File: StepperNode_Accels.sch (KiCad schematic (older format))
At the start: 0 parts

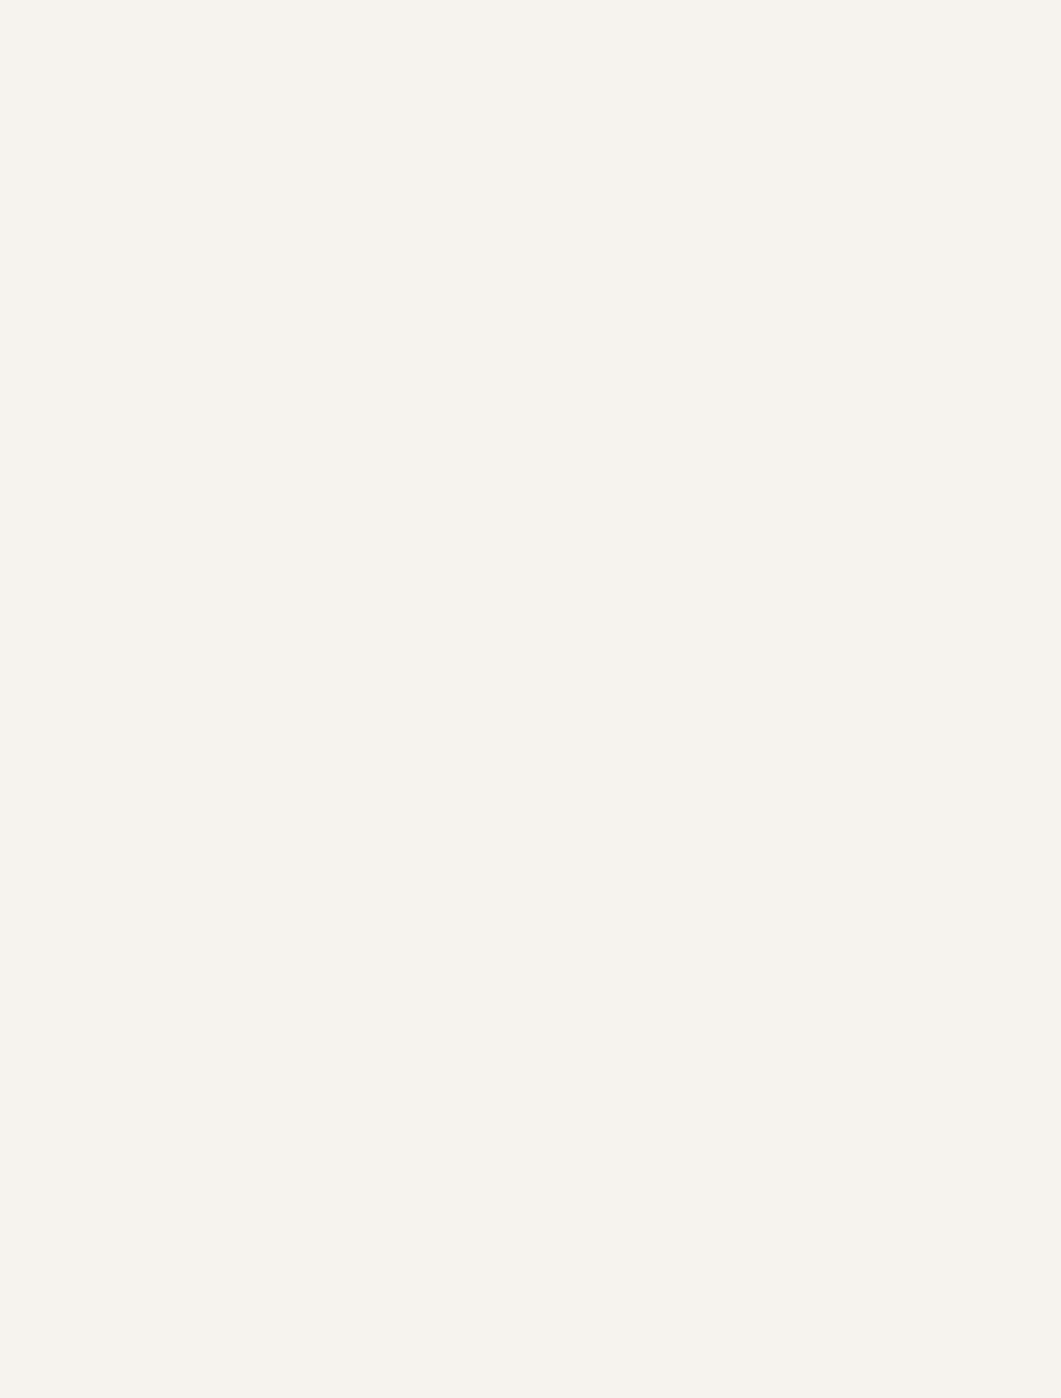
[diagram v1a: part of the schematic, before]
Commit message: Added Brake Failsafe Sheet
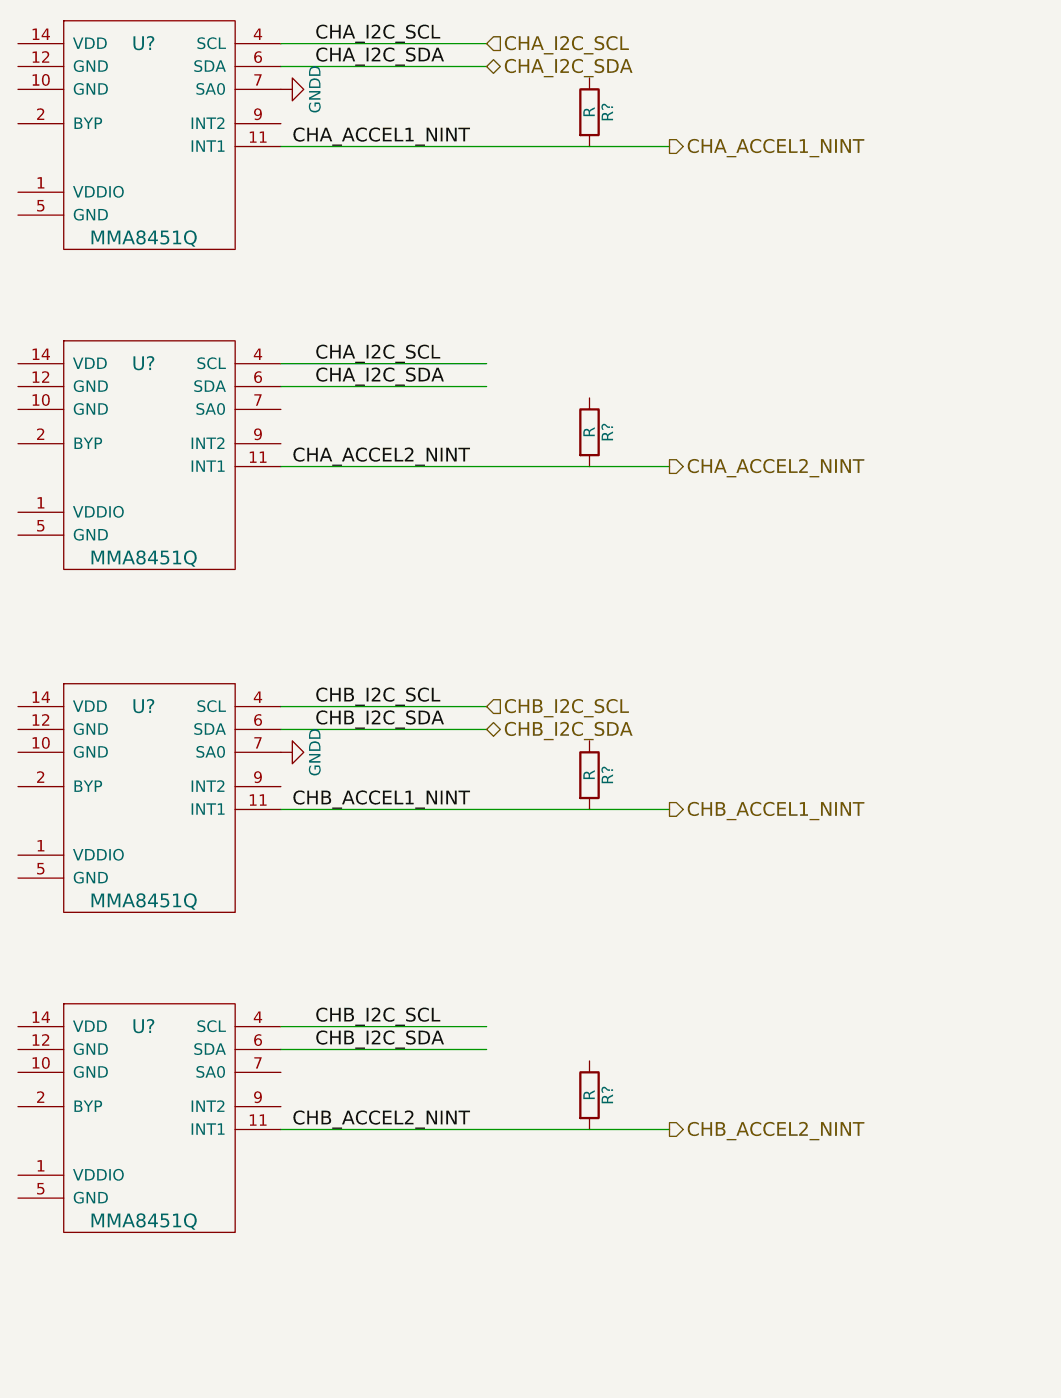
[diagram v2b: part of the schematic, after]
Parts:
- added R? (x4): R, symbol R
- added U? (x4): MMA8451Q, symbol MMA8451Q
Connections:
- net labels added: CHA_ACCEL1_NINT, CHA_ACCEL2_NINT, CHA_I2C_SCL, CHA_I2C_SDA, CHB_ACCEL1_NINT, CHB_ACCEL2_NINT, CHB_I2C_SCL, CHB_I2C_SDA, GNDD
- wire segments 0 -> 12
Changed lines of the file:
@@
 $Descr A3 16535 11693
 encoding utf-8
-Sheet 12 13
+Sheet 12 14
 Title "Accelerometers"
 Date ""
@@
 Text Notes 11950 10500 0    60   ~ 0
 Original Author: SafetyLok
+$Comp
+L MMA8451Q U?
+U 1 1 5753CAE0
+P 5300 2200
+F 0 "U?" H 5300 2700 60  0000 C CNN
+F 1 "MMA8451Q" H 5300 1850 60  0000 C CNN
+F 2 "" H 5300 2200 60  0000 C CNN
+F 3 "" H 5300 2200 60  0000 C CNN
+	1    5300 2200
+	1    0    0    -1
+$EndComp
+Wire Wire Line
+	5900 1700 6800 1700
+Wire Wire Line
+	5900 1800 6800 1800
+Text Label 6050 1700 0    60   ~ 0
+CHA_I2C_SCL
+Text Label 6050 1800 0    60   ~ 0
+CHA_I2C_SDA
+Wire Wire Line
+	5900 2150 7600 2150
+Text Label 5950 2150 0    60   ~ 0
+CHA_ACCEL1_NINT
+$Comp
+L R R?
+U 1 1 5753CBA8
+P 7250 2000
+F 0 "R?" V 7330 2000 50  0000 C CNN
+F 1 "R" V 7250 2000 50  0000 C CNN
+F 2 "" V 7180 2000 50  0000 C CNN
+F 3 "" H 7250 2000 50  0000 C CNN
+	1    7250 2000
+	1    0    0    -1
+$EndComp
+$Comp
+L MMA8451Q U?
+U 1 1 5753CD7B
+P 5300 3600
+F 0 "U?" H 5300 4100 60  0000 C CNN
+F 1 "MMA8451Q" H 5300 3250 60  0000 C CNN
+F 2 "" H 5300 3600 60  0000 C CNN
+F 3 "" H 5300 3600 60  0000 C CNN
+	1    5300 3600
+	1    0    0    -1
+$EndComp
+Wire Wire Line
+	5900 3100 6800 3100
+Wire Wire Line
+	5900 3200 6800 3200
+Text Label 6050 3100 0    60   ~ 0
+CHA_I2C_SCL
+Text Label 6050 3200 0    60   ~ 0
+CHA_I2C_SDA
+Wire Wire Line
+	5900 3550 7600 3550
+Text Label 5950 3550 0    60   ~ 0
+CHA_ACCEL2_NINT
+$Comp
+L R R?
+U 1 1 5753CD87
+P 7250 3400
+F 0 "R?" V 7330 3400 50  0000 C CNN
+F 1 "R" V 7250 3400 50  0000 C CNN
+F 2 "" V 7180 3400 50  0000 C CNN
+F 3 "" H 7250 3400 50  0000 C CNN
+	1    7250 3400
+	1    0    0    -1
+$EndComp
+$Comp
+L MMA8451Q U?
+U 1 1 5753CF5A
+P 5300 5100
+F 0 "U?" H 5300 5600 60  0000 C CNN
+F 1 "MMA8451Q" H 5300 4750 60  0000 C CNN
+F 2 "" H 5300 5100 60  0000 C CNN
+F 3 "" H 5300 5100 60  0000 C CNN
+	1    5300 5100
+	1    0    0    -1
+$EndComp
+Wire Wire Line
+	5900 4600 6800 4600
+Wire Wire Line
+	5900 4700 6800 4700
+Text Label 6050 4600 0    60   ~ 0
+CHB_I2C_SCL
+Text Label 6050 4700 0    60   ~ 0
+CHB_I2C_SDA
+Wire Wire Line
+	5900 5050 7600 5050
+Text Label 5950 5050 0    60   ~ 0
+CHB_ACCEL1_NINT
+$Comp
+L R R?
+U 1 1 5753CF66
+P 7250 4900
+F 0 "R?" V 7330 4900 50  0000 C CNN
+F 1 "R" V 7250 4900 50  0000 C CNN
+F 2 "" V 7180 4900 50  0000 C CNN
+F 3 "" H 7250 4900 50  0000 C CNN
+	1    7250 4900
+	1    0    0    -1
+$EndComp
+$Comp
+L MMA8451Q U?
+U 1 1 5753CF6C
+P 5300 6500
+F 0 "U?" H 5300 7000 60  0000 C CNN
+F 1 "MMA8451Q" H 5300 6150 60  0000 C CNN
+F 2 "" H 5300 6500 60  0000 C CNN
+F 3 "" H 5300 6500 60  0000 C CNN
+	1    5300 6500
+	1    0    0    -1
+$EndComp
+Wire Wire Line
+	5900 6000 6800 6000
+Wire Wire Line
+	5900 6100 6800 6100
+Text Label 6050 6000 0    60   ~ 0
+CHB_I2C_SCL
+Text Label 6050 6100 0    60   ~ 0
+CHB_I2C_SDA
+Wire Wire Line
+	5900 6450 7600 6450
+Text Label 5950 6450 0    60   ~ 0
+CHB_ACCEL2_NINT
+$Comp
+L R R?
+U 1 1 5753CF78
+P 7250 6300
+F 0 "R?" V 7330 6300 50  0000 C CNN
+F 1 "R" V 7250 6300 50  0000 C CNN
+F 2 "" V 7180 6300 50  0000 C CNN
+F 3 "" H 7250 6300 50  0000 C CNN
+	1    7250 6300
+	1    0    0    -1
+$EndComp
+Text HLabel 6800 1700 2    60   Input ~ 0
+CHA_I2C_SCL
+Text HLabel 6800 1800 2    60   BiDi ~ 0
+CHA_I2C_SDA
+Text HLabel 7600 2150 2    60   Output ~ 0
+CHA_ACCEL1_NINT
+Text HLabel 7600 3550 2    60   Output ~ 0
+CHA_ACCEL2_NINT
+Text HLabel 7600 5050 2    60   Output ~ 0
+CHB_ACCEL1_NINT
+Text HLabel 7600 6450 2    60   Output ~ 0
+CHB_ACCEL2_NINT
+$Comp
+L GNDD #PWR?
+U 1 1 5753D35F
+P 5900 4800
+F 0 "#PWR?" H 5900 4550 50  0001 C CNN
+F 1 "GNDD" H 5900 4650 50  0000 C CNN
+F 2 "" H 5900 4800 50  0000 C CNN
+F 3 "" H 5900 4800 50  0000 C CNN
+	1    5900 4800
+	0    -1   -1   0
+$EndComp
+$Comp
+L GNDD #PWR?
+U 1 1 5753D40B
+P 5900 1900
+F 0 "#PWR?" H 5900 1650 50  0001 C CNN
+F 1 "GNDD" H 5900 1750 50  0000 C CNN
+F 2 "" H 5900 1900 50  0000 C CNN
+F 3 "" H 5900 1900 50  0000 C CNN
+	1    5900 1900
+	0    -1   -1   0
+$EndComp
+Text HLabel 6800 4600 2    60   Input ~ 0
+CHB_I2C_SCL
+Text HLabel 6800 4700 2    60   BiDi ~ 0
+CHB_I2C_SDA
 $EndSCHEMATC

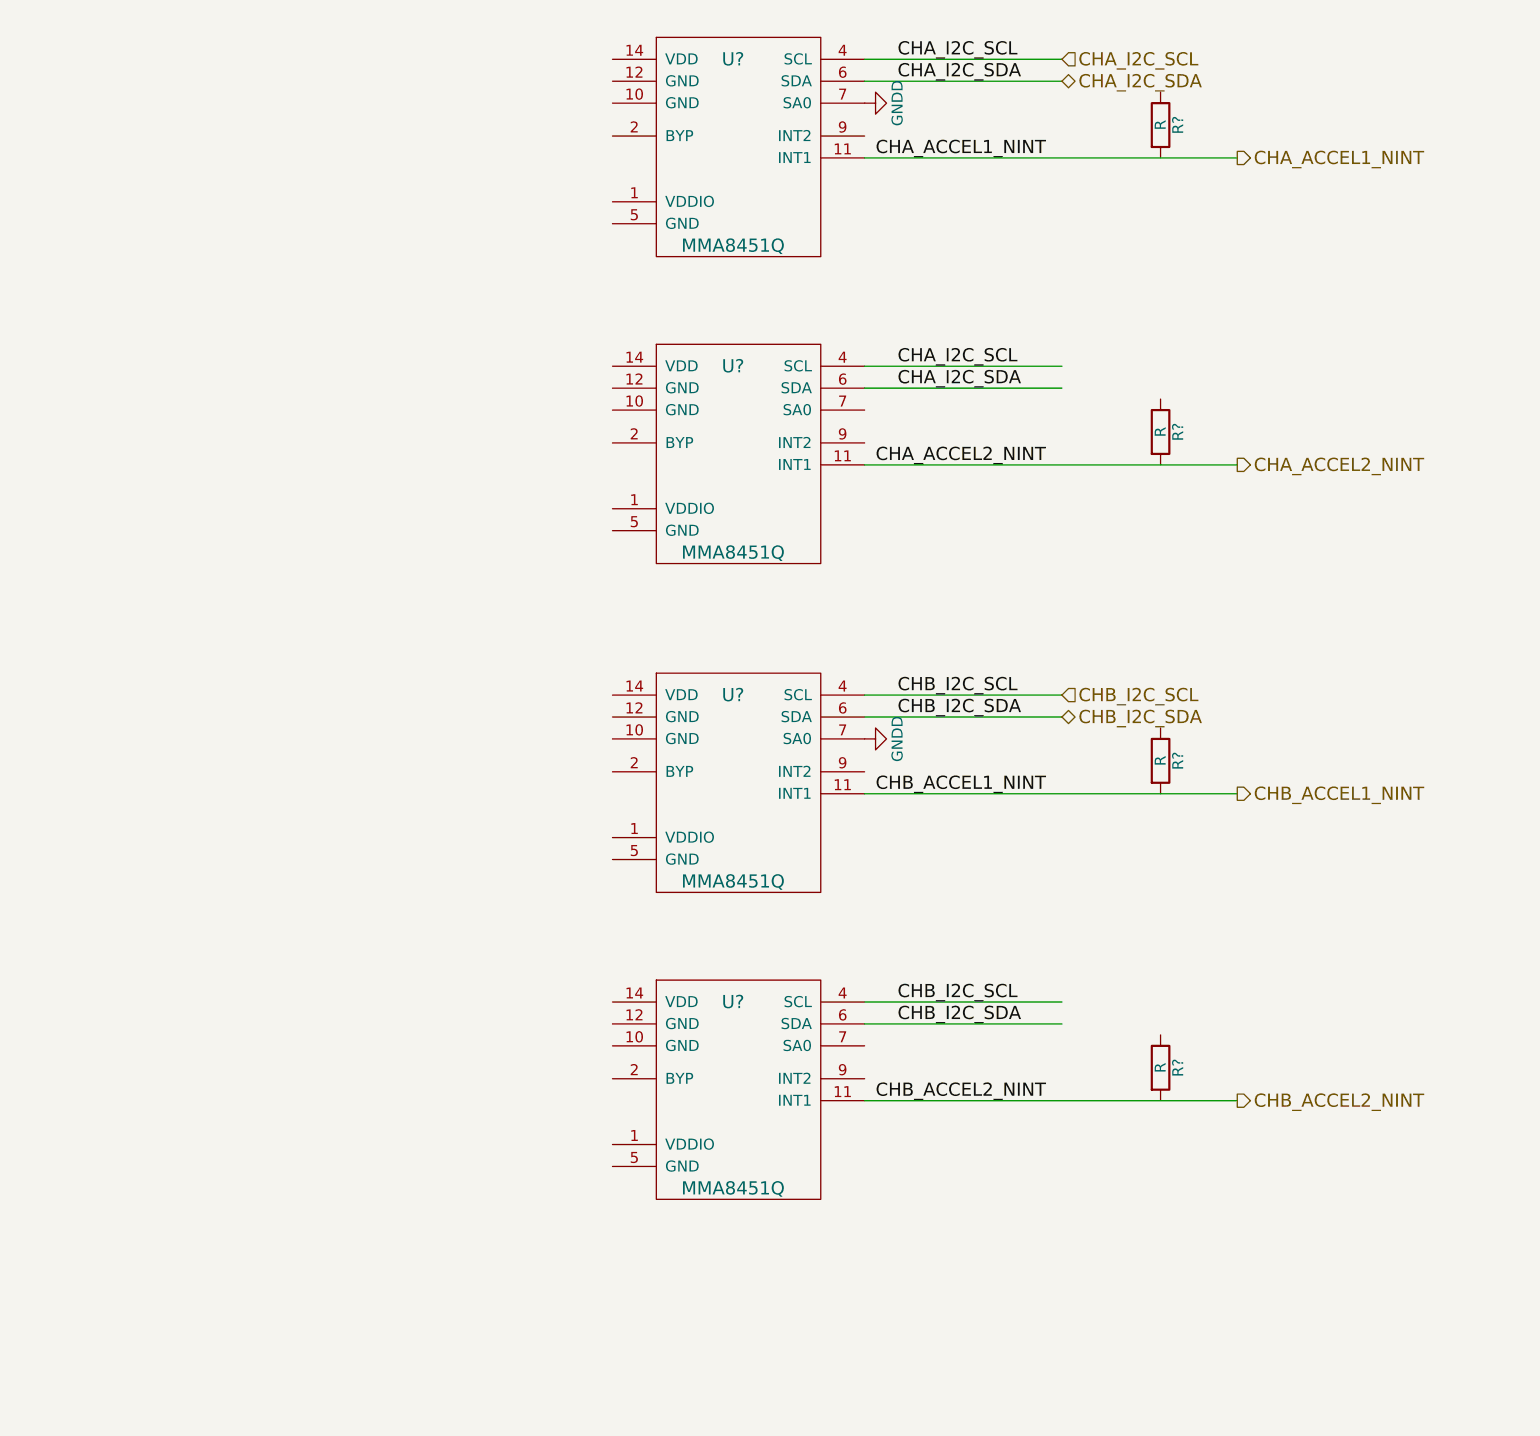
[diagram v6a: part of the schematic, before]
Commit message: Update Stepper Temp Sensor Interface
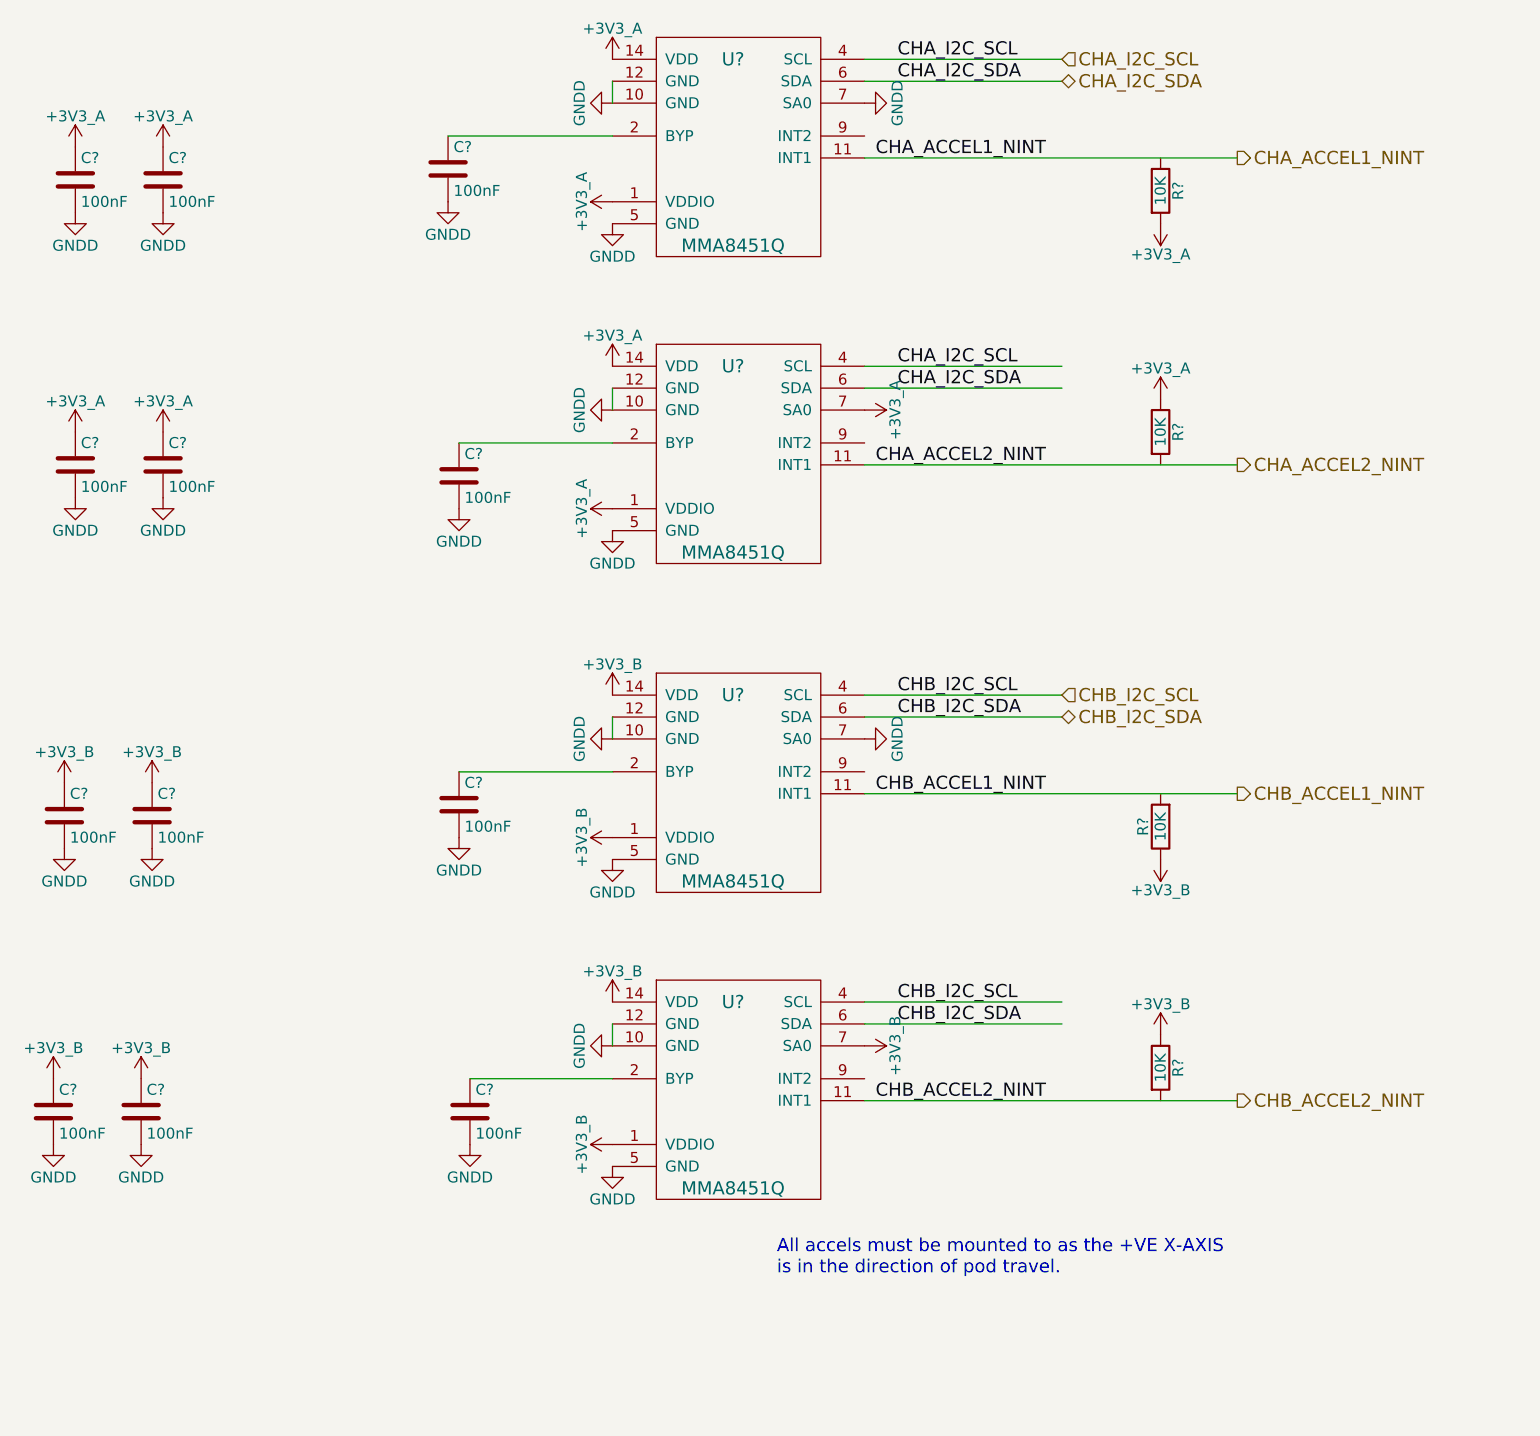
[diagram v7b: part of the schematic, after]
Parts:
- added C? (x12): 100nF, symbol C
- R? (x4): value R -> 10K
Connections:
- net labels added: +3V3_A, +3V3_B
- wire segments 12 -> 20
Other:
- note added: "All accels must be mounted to as the +VE X-AXIS \nis in the direction of pod travel.\n"
- moved on the sheet: R?
